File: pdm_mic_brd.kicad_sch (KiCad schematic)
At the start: 47 parts, among them J1 V_SET_JMP, J10 LEFT_BIAS_JMP, J11 RIGHT_BIAS_JMP, J12 RT_IN_SEL, J13 LEFT_IN_SEL, J14 RIGHT_SMA, J15 LEFT_SMA, J16 AudioJack3, J2 USB_B_Micro, J3 CLOCK_SMA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

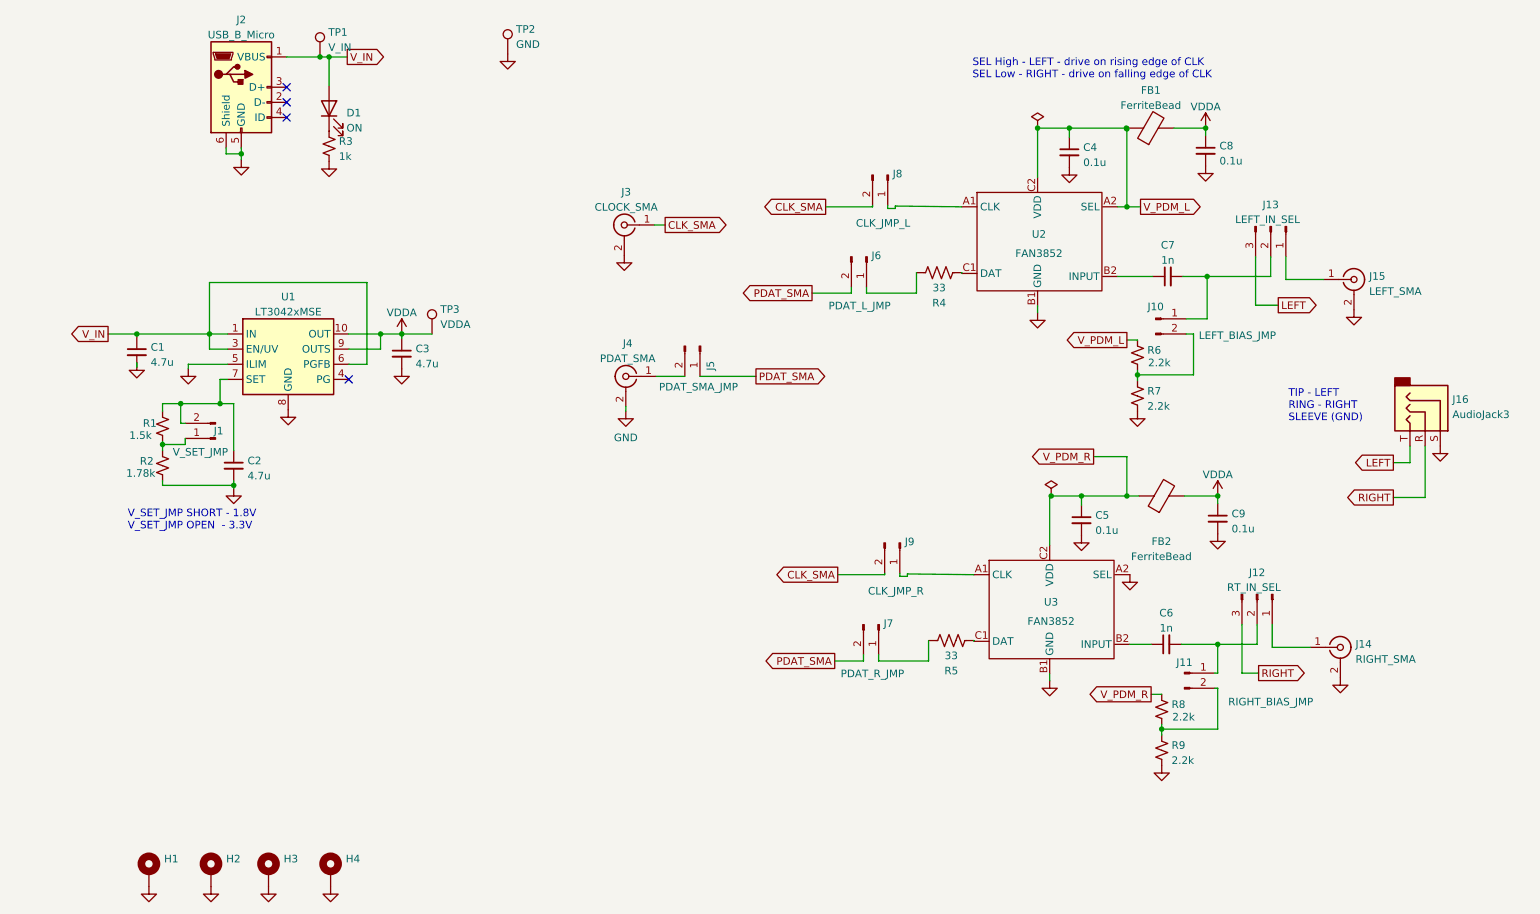
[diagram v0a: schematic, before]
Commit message: fix R1, R2 values
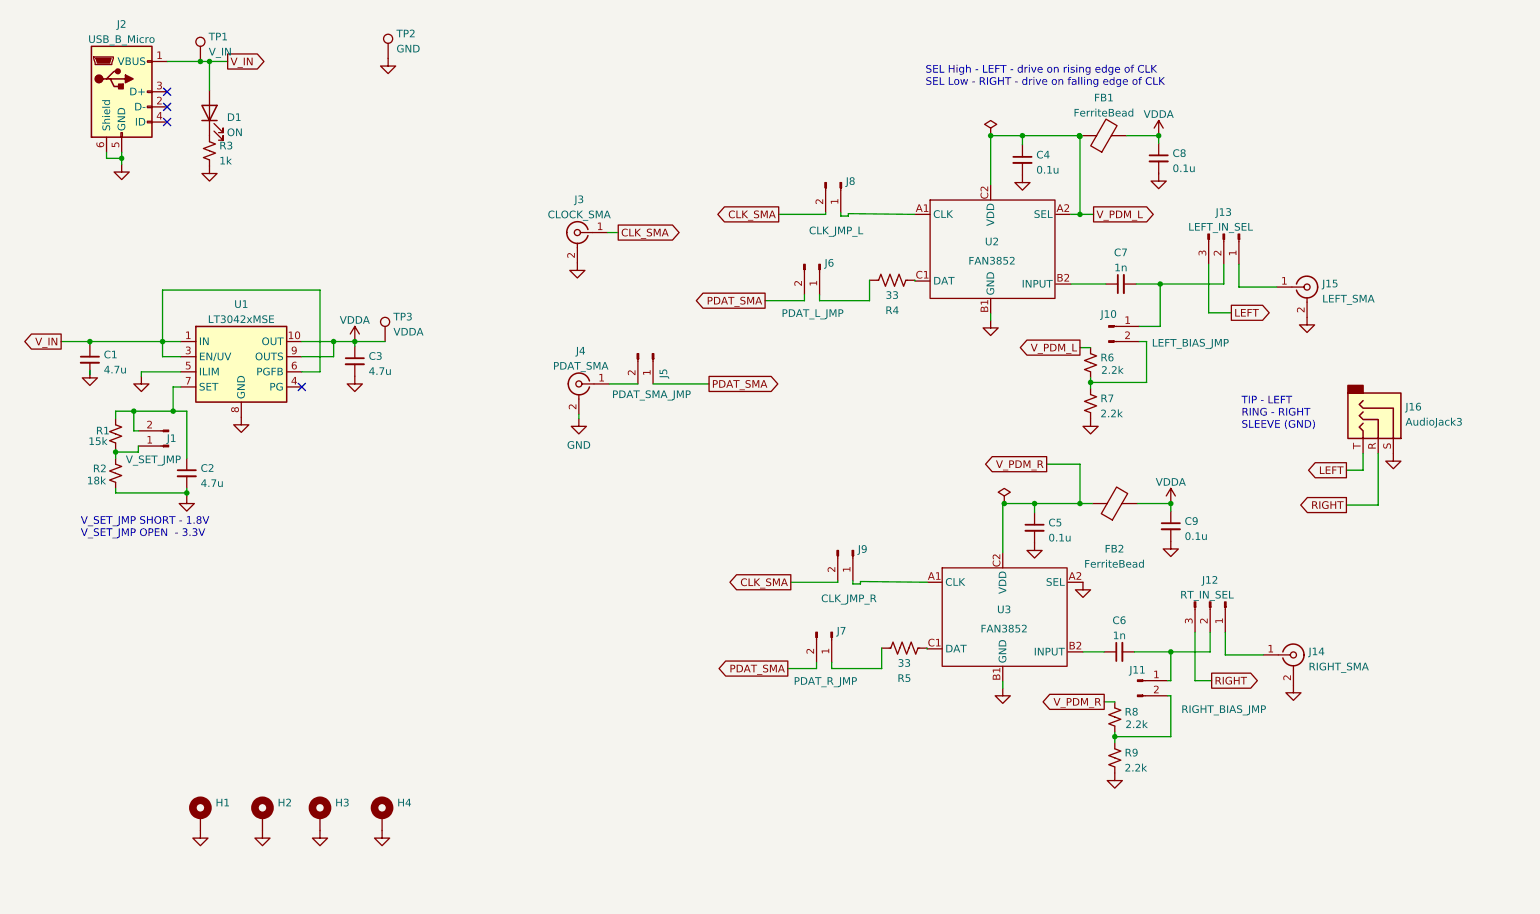
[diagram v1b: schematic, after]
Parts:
- R1: value 1.5k -> 15k
- R2: value 1.78k -> 18k
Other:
- moved on the sheet: C1, C2, C3, C4, C5, C6, C7, C8, C9, D1, FB1, FB2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
